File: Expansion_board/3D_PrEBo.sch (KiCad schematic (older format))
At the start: 73 parts, among them J1 LED, J10 TMC_INPUT, J11 Power_out, J12 Z_Probe, J13 Fan_interconnection_header, J14 X_MIN, J15 Z_MAX, J2 V_IN, J3 RJ45, J4 X, J5 Y, J6 Z, J7 E0, J8 E1, J9 FAN&LED_INPUT, M1 Fan_3pin, M2 Fan_3pin, M3 Fan_3pin, M4 Fan_3pin, M5 Fan_3pin, M6 Fan_3pin, M7 Fan_3pin, M8 Fan_4pin, Q1 AOD4189, Q10 IRLML2502, Q2 IRLML2502, Q3 IRLML2502, Q4 IRLML2502, Q5 IRLML2502, Q6 IRLML2502, Q7 IRLML2502, Q8 IRLML2502, Q9 IRLML2502, U1 L5973D, U2 NCP1117-5.0_SOT223

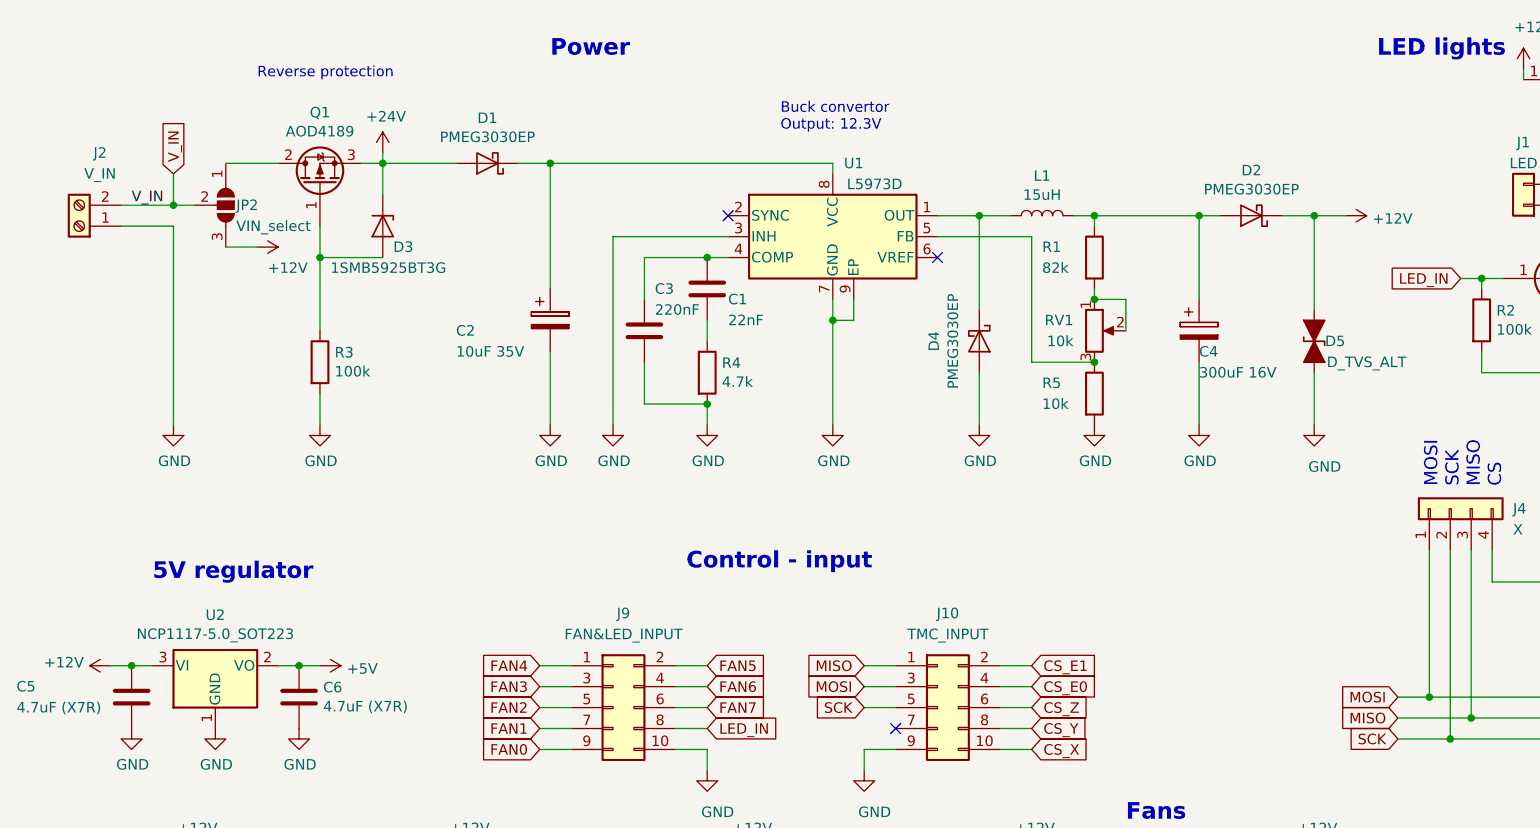
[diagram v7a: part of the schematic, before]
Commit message: Expansion_board: Add test points for voltages
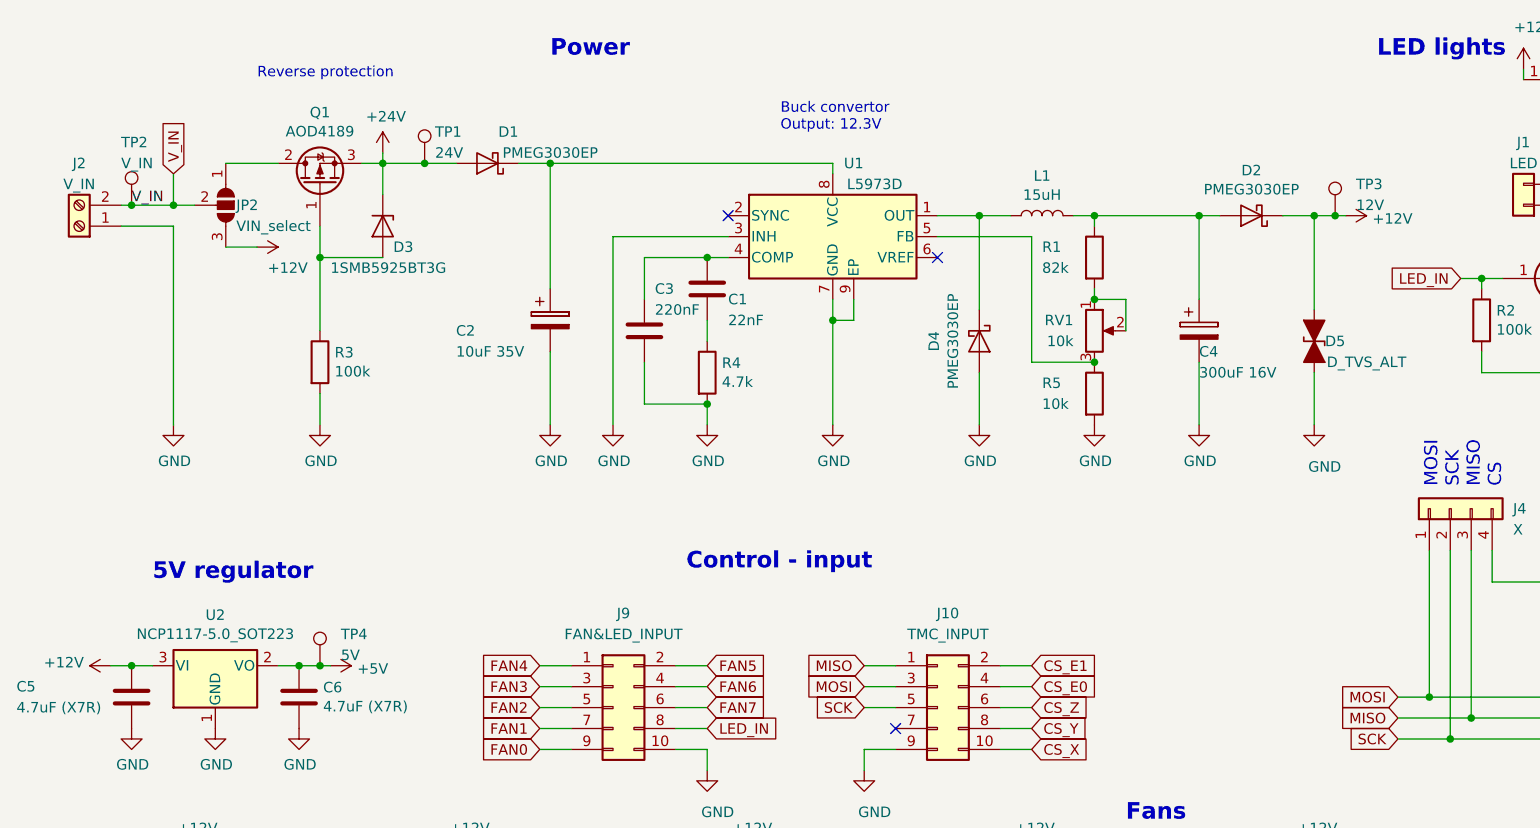
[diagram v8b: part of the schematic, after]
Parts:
- added TP1: 24V, TestPoint:TestPoint_THTPad_D1.5mm_Drill0.7mm, symbol Connector:TestPoint
- added TP2: V_IN, TestPoint:TestPoint_THTPad_D1.5mm_Drill0.7mm, symbol Connector:TestPoint
- added TP3: 12V, TestPoint:TestPoint_THTPad_D1.5mm_Drill0.7mm, symbol Connector:TestPoint
- added TP4: 5V, TestPoint:TestPoint_THTPad_D1.5mm_Drill0.7mm, symbol Connector:TestPoint
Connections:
- net +12V: now also TP3.1
- net +24V: now also TP1.1
- net +5V: now also TP4.1
- net V_IN: now also TP2.1
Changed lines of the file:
@@
 U 1 1 5C5ABFBD
 P 2750 1300
-F 0 "D1" H 2750 1084 50  0000 C CNN
-F 1 "PMEG3030EP" H 2750 1175 50  0000 C CNN
+F 0 "D1" H 2650 1150 50  0000 C CNN
+F 1 "PMEG3030EP" H 2450 1250 50  0000 C CNN
 F 2 "Diode_SMD:D_SMB" H 2750 1300 50  0001 C CNN
 F 3 "~" H 2750 1300 50  0001 C CNN
@@
 Connection ~ 2250 1300
 Wire Wire Line
-	2250 1300 2600 1300
+	2250 1300 2450 1300
 Text Label 1050 1500 0    50   ~ 0
 V_IN
@@
 L power:+5V #PWR019
 U 1 1 5C617DDA
-P 1950 3700
-F 0 "#PWR019" H 1950 3550 50  0001 C CNN
-F 1 "+5V" V 1965 3828 50  0000 L CNN
-F 2 "" H 1950 3700 50  0001 C CNN
-F 3 "" H 1950 3700 50  0001 C CNN
-	1    1950 3700
+P 2000 3700
+F 0 "#PWR019" H 2000 3550 50  0001 C CNN
+F 1 "+5V" V 2015 3828 50  0000 L CNN
+F 2 "" H 2000 3700 50  0001 C CNN
+F 3 "" H 2000 3700 50  0001 C CNN
+	1    2000 3700
 	0    1    1    0
 $EndComp
@@
 U 1 1 5CE56BA2
 P 800 1600
-F 0 "J2" H 700 1250 50  0000 C CNN
-F 1 "V_IN" H 700 1350 50  0000 C CNN
+F 0 "J2" H 800 1300 50  0000 C CNN
+F 1 "V_IN" H 800 1400 50  0000 C CNN
 F 2 "TerminalBlock_Phoenix:TerminalBlock_Phoenix_MKDS-1,5-2_1x02_P5.00mm_Horizontal" H 800 1600 50  0001 C CNN
 F 3 "~" H 800 1600 50  0001 C CNN
@@
 	1250 1600 1250 2550
 Wire Wire Line
-	1000 1500 1250 1500
+	1000 1500 1050 1500
 Wire Wire Line
 	1500 1300 1750 1300
@@
 Connection ~ 6700 1550
 Wire Wire Line
-	6700 1550 6850 1550
+	6700 1550 6800 1550
 Wire Wire Line
 	6700 2300 6700 2550
@@
 	1    0    0    -1
 $EndComp
+$Comp
+L Connector:TestPoint TP1
+U 1 1 5C62C948
+P 2450 1300
+F 0 "TP1" H 2500 1450 50  0000 L CNN
+F 1 "24V" H 2500 1350 50  0000 L CNN
+F 2 "TestPoint:TestPoint_THTPad_D1.5mm_Drill0.7mm" H 2650 1300 50  0001 C CNN
+F 3 "~" H 2650 1300 50  0001 C CNN
+	1    2450 1300
+	1    0    0    -1
+$EndComp
+Connection ~ 2450 1300
+Wire Wire Line
+	2450 1300 2600 1300
+$Comp
+L Connector:TestPoint TP3
+U 1 1 5C62DFCF
+P 6800 1550
+F 0 "TP3" H 6900 1700 50  0000 L CNN
+F 1 "12V" H 6900 1600 50  0000 L CNN
+F 2 "TestPoint:TestPoint_THTPad_D1.5mm_Drill0.7mm" H 7000 1550 50  0001 C CNN
+F 3 "~" H 7000 1550 50  0001 C CNN
+	1    6800 1550
+	1    0    0    -1
+$EndComp
+Connection ~ 6800 1550
+Wire Wire Line
+	6800 1550 6850 1550
+$Comp
+L Connector:TestPoint TP4
+U 1 1 5C62E4E5
+P 1950 3700
+F 0 "TP4" H 2050 3850 50  0000 L CNN
+F 1 "5V" H 2050 3750 50  0000 L CNN
+F 2 "TestPoint:TestPoint_THTPad_D1.5mm_Drill0.7mm" H 2150 3700 50  0001 C CNN
+F 3 "~" H 2150 3700 50  0001 C CNN
+	1    1950 3700
+	1    0    0    -1
+$EndComp
+Connection ~ 1950 3700
+Wire Wire Line
+	2000 3700 1950 3700
+$Comp
+L Connector:TestPoint TP2
+U 1 1 5C646B91
+P 1050 1500
+F 0 "TP2" H 1000 1800 50  0000 L CNN
+F 1 "V_IN" H 1000 1700 50  0000 L CNN
+F 2 "TestPoint:TestPoint_THTPad_D1.5mm_Drill0.7mm" H 1250 1500 50  0001 C CNN
+F 3 "~" H 1250 1500 50  0001 C CNN
+	1    1050 1500
+	1    0    0    -1
+$EndComp
+Connection ~ 1050 1500
+Wire Wire Line
+	1050 1500 1250 1500
 $EndSCHEMATC
